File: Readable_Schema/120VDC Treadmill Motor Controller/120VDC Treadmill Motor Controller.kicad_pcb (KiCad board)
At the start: 4 copper layers, 186.8 x 133.2 mm, 149 parts, among them J1 TB005-762-03BE, J2 OSTT7020150, J3 TB0011-350-08BE, J4 TB0011-350-08BE, J5 TB0011-350-08BE, J6 TB0011-350-03BE, J7 OSTT7020150, J9 OSTT7020150, K1 T9GV1L14-24, Q1 IPP200N25N3 G, Q2 IPP200N25N3 G, Q3 IPP200N25N3 G, Q4 IPP200N25N3 G, Q5 IPP200N25N3 G, Q7 DN2450N8-G, Q8 VOM1271T, U1 UCC21530DWKR, U2 UCC21530DWKR, U3 TMCS1126B42QDVGRQ1, U4 SN74HCS08DYYR, U5 TPSI3050QDWZRQ1, U6 AMC1311BDWVR

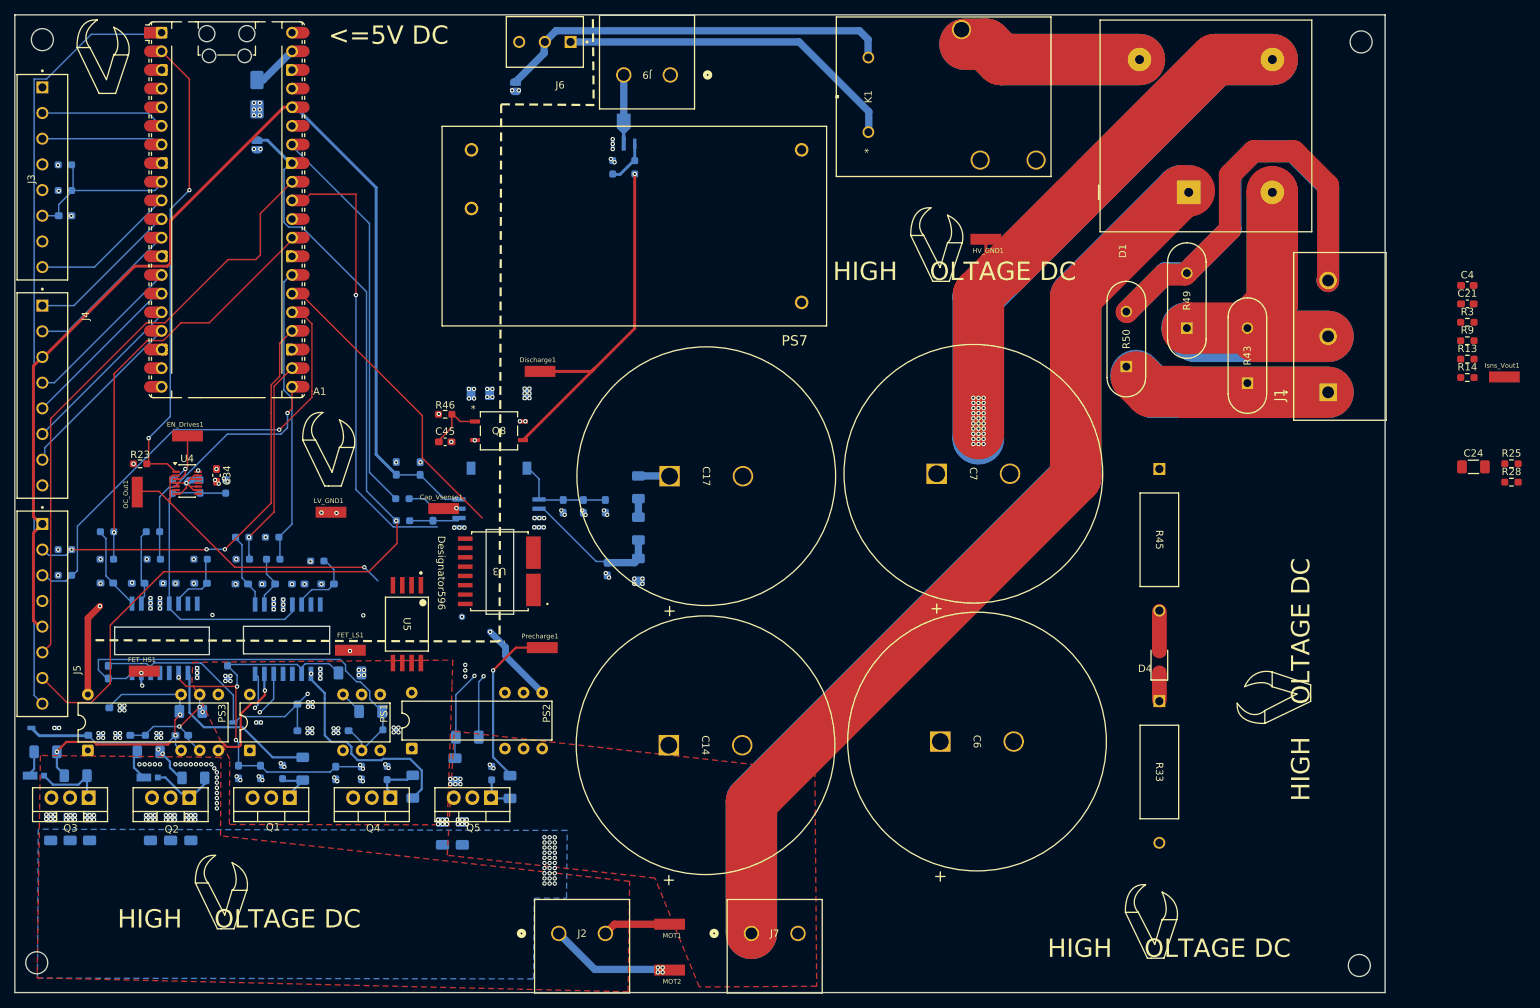
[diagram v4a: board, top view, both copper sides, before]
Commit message: -Finished refactoring the 20amp traces to work with a 4 layer 1oz board. -Working on reconnecting some of the smaller components after some of the moves needed to achieve line 1
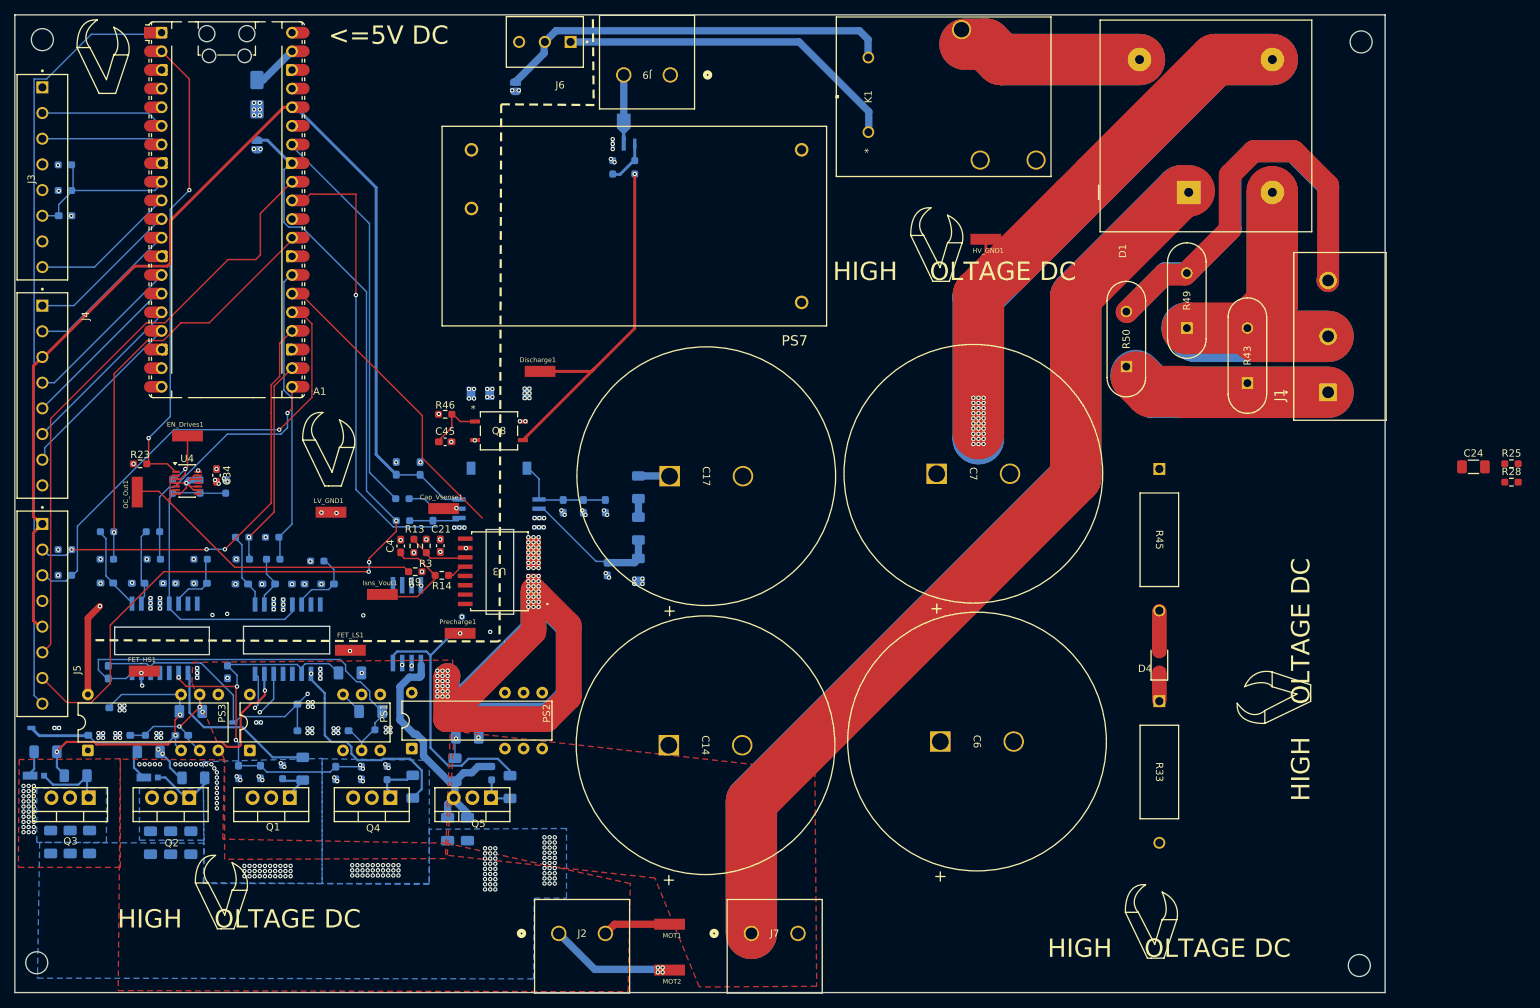
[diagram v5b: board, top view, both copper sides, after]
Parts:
- U5: moved to B.Cu
- moved Isns_Vout1 155.8 mm to (66.6, 124.8)
- moved C4 149.7 mm to (69.1, 118.2), turned to 90 degrees
- moved R9 146.8 mm to (71.1, 121.7)
- moved R13 145.8 mm to (70.9, 118.2), turned to 90 degrees
- moved R3 145.1 mm to (72.6, 118.2), turned to 90 degrees
- moved C21 143.8 mm to (74.5, 118.2), turned to -90 degrees
- moved R14 142.3 mm to (74.7, 122.2), turned to 180 degrees
- moved Precharge1 11.4 mm to (77.2, 130.1)
- moved C32 1.88 mm to (35.0, 158.6)
- moved C51 1.88 mm to (37.8, 158.6)
- moved C52 1.88 mm to (40.5, 158.6)
- moved C28 1.78 mm to (26.7, 158.5)
- moved C49 1.78 mm to (21.4, 158.5)
- moved C50 1.78 mm to (24.1, 158.5)
- moved R7 1.09 mm to (66.5, 143.2)
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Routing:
- net /Feedback/in+: track 0.00 -> 123.0 mm, vias 18 -> 57
- net HV_GND: track 153.6 -> 196.2 mm, vias 99 -> 114
- net 170V Rect: track 3.79 -> 39.6 mm, vias 59 -> 27
- net Net-(U5-VDRV): track 22.7 -> 37.2 mm
- net /Feedback/v_out: track 61.1 -> 74.0 mm
- net Net-(U5-VDDH): track 8.57 -> 19.5 mm, vias 1 -> 2
- net Net-(U3-VOC): track 0.00 -> 7.66 mm
- net Net-(U5-VDDM): track 12.1 -> 18.3 mm, vias 1 -> 2
- net /Feedback/OC_out: track 41.5 -> 45.2 mm, vias 1 -> 0
- net Net-(U3-VOUT): track 0.00 -> 2.27 mm
- net /H_Bridge/hs_ps_1_+: track 59.2 -> 58.0 mm
- net /Feedback/adc_gnd: track 128.3 -> 128.2 mm, vias 1 -> 3
- net LV_GND: track 46.9 -> 46.8 mm, vias 48 -> 52
- net Net-(J2-Pin_2): vias 40 -> 70
- net Net-(J2-Pin_1): vias 22 -> 82
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- added copper zone on B.Cu, net 170V Rect
- added copper zone on B.Cu, net Net-(J2-Pin_1)
- added copper zone on F.Cu, net Net-(J2-Pin_1)
- added copper zone on B.Cu, net Net-(J2-Pin_2)

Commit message: -Finished refactoring for larger minimum board fills and trace sizes -Doing some peer reviews then searching for the best available price online
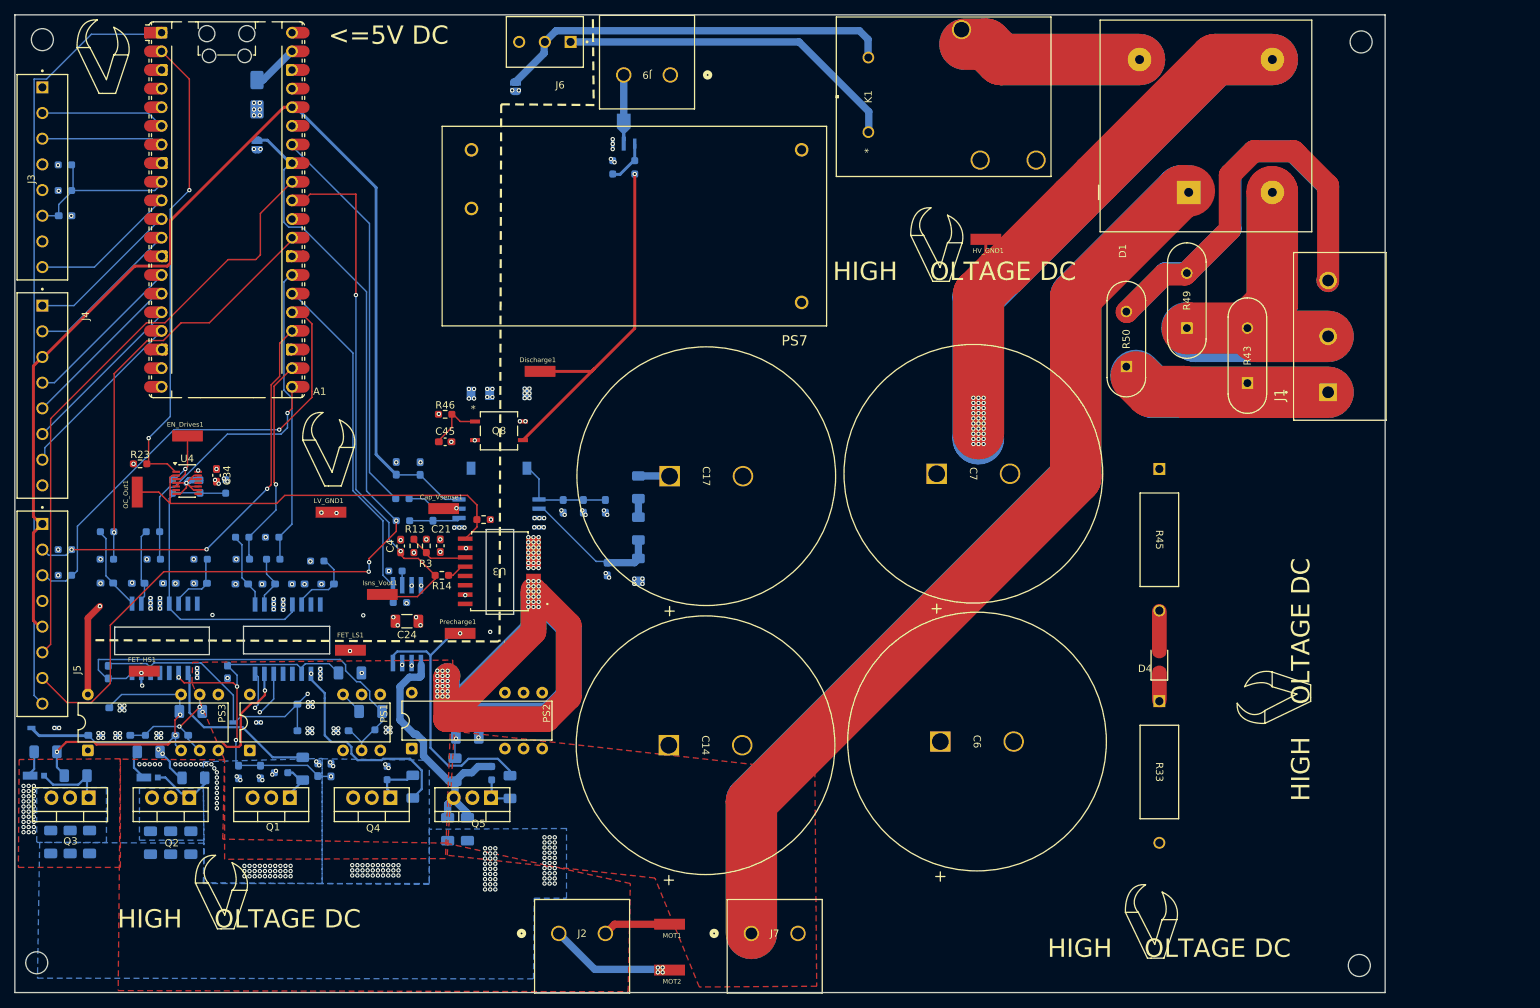
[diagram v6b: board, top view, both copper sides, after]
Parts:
- R25, R28: moved to B.Cu
- moved R25 152.8 mm to (68.4, 121.6), turned to 180 degrees
- moved R28 152.4 mm to (69.0, 125.9)
- moved C24 146.9 mm to (70.0, 128.4), turned to 180 degrees
- moved R9 11.7 mm to (80.4, 114.6)
- moved C43 4.17 mm to (59.6, 148.7), turned to 90 degrees
- moved C20 2.49 mm to (57.8, 148.7), turned to 90 degrees
- moved R17 0.22 mm to (52.8, 149.1), turned to 0 degrees
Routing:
- net /Feedback/OC_out: track 45.2 -> 57.3 mm
- net /Pi Pico/pre_charge_mcu: track 42.0 -> 48.7 mm
- net 5v 15w: track 41.3 -> 36.0 mm
- net /Feedback/v_out: track 74.0 -> 71.7 mm, vias 1 -> 2
- net Net-(U5-PXFR): track 0.00 -> 1.74 mm
- net Net-(A1-GPIO18): track 58.7 -> 57.2 mm
- net Net-(Q1-G): track 6.38 -> 5.80 mm
- net /H_Bridge/ls_ps_+: track 81.3 -> 81.2 mm, vias 5 -> 4
- net LV_GND: vias 52 -> 57
- net /Feedback/in+: vias 57 -> 54

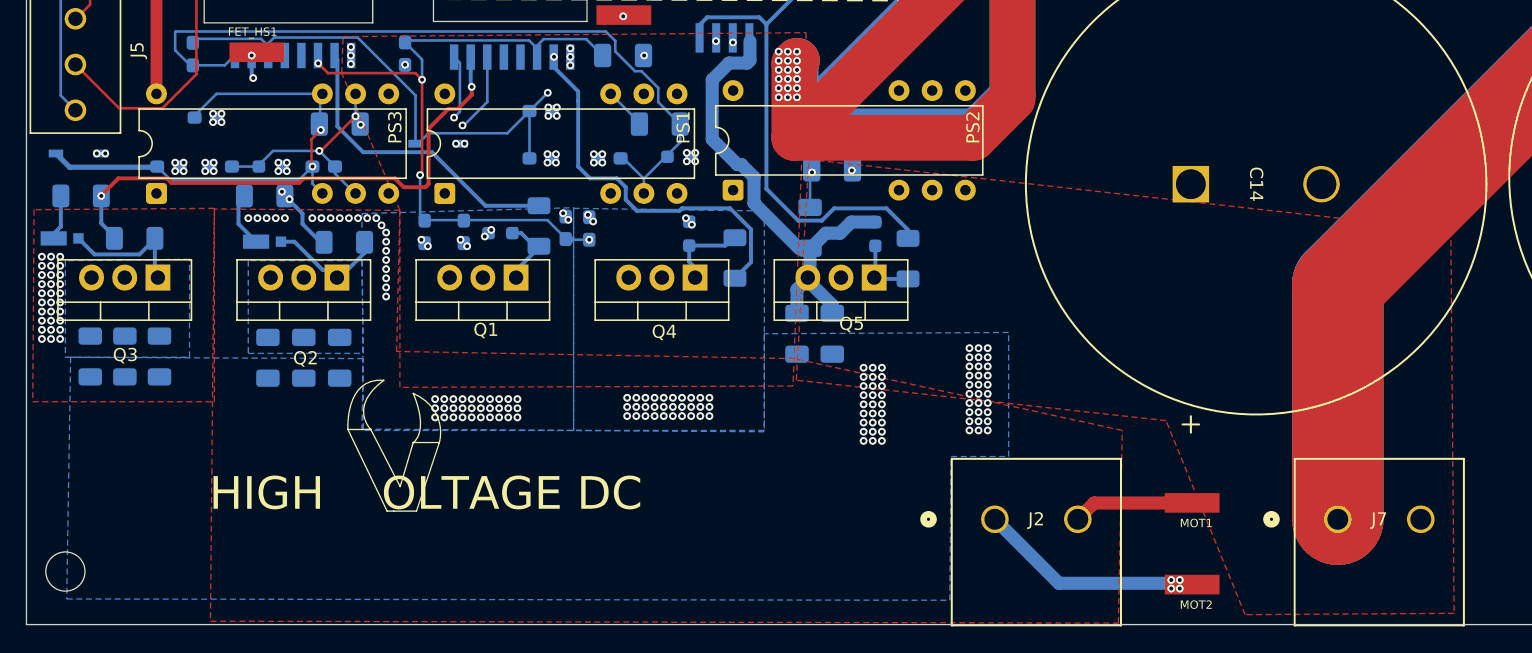
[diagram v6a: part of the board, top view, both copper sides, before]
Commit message: -Fixed some more of the high current carrying capacity traces and board fills -Reduced the number of vias being used to jump between layers to allow for wider board fills
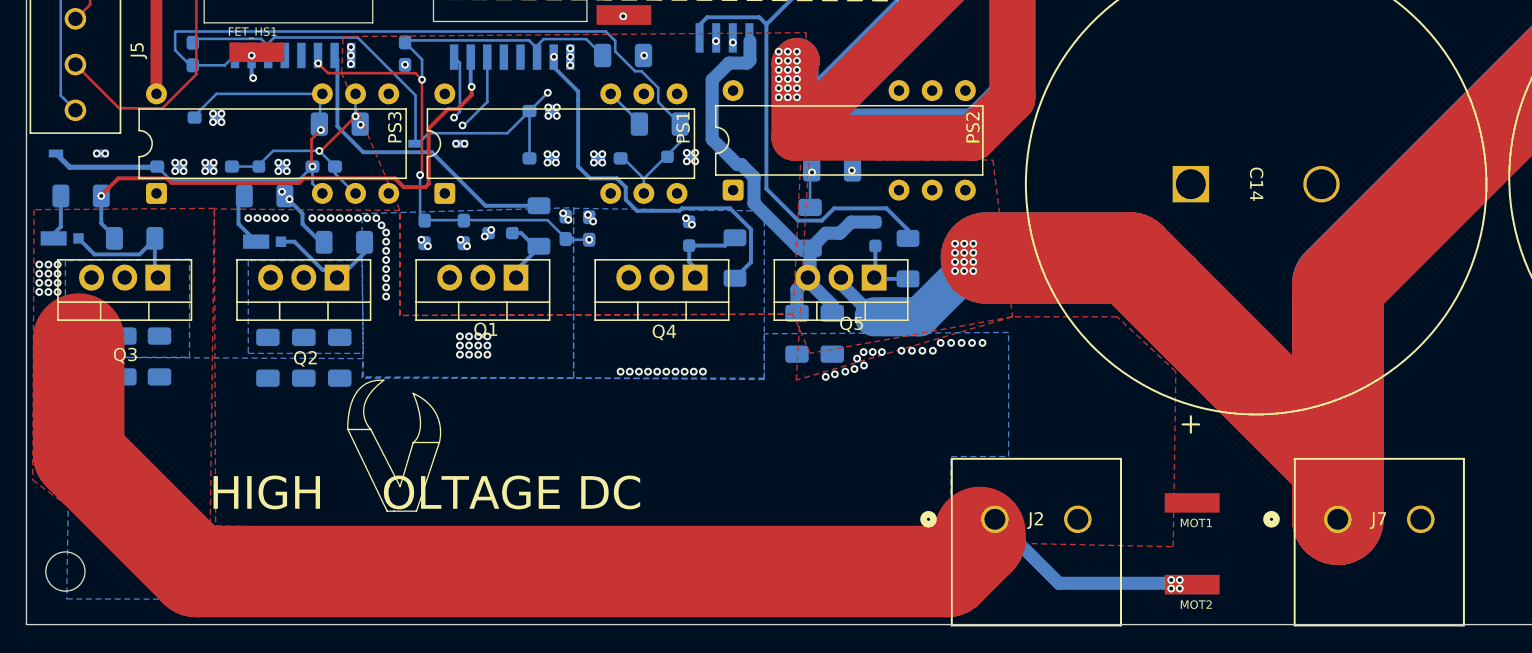
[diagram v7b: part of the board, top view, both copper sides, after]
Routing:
- net Net-(D1-+): track 253.0 -> 339.6 mm, vias 0 -> 12
- net Net-(J2-Pin_1): track 15.8 -> 98.9 mm, vias 82 -> 44
- net Net-(J2-Pin_2): track 9.06 -> 0.00 mm, vias 70 -> 52
- net HV_GND: vias 114 -> 93
- net 170V Rect: vias 27 -> 9
